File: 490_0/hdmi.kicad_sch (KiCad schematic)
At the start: 6 parts, among them J19 467650301, U10 EMI8142MUTAG, U13 SP3003-02XTG, U14 SP3003-02XTG, U9 EMI8142MUTAG

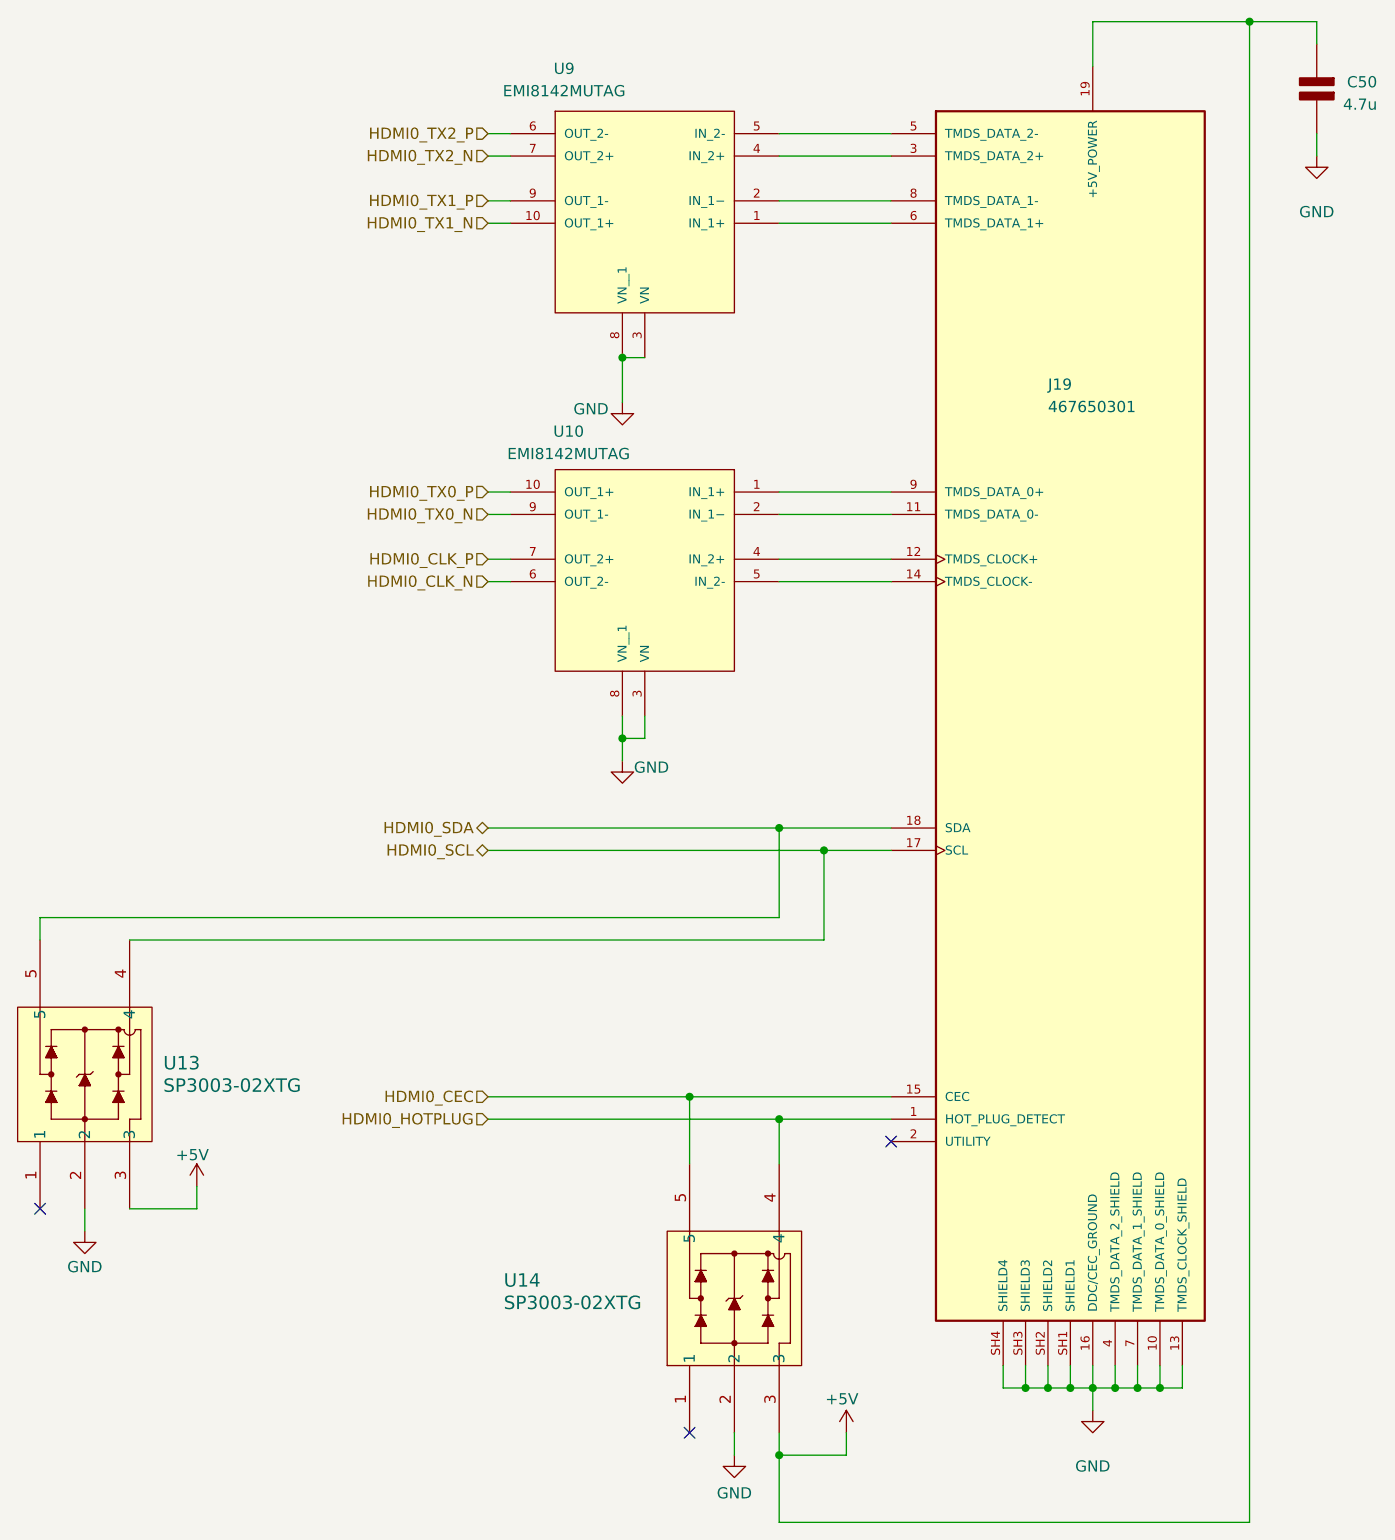
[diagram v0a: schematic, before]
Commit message: Changed microHDMI to normal HDMI because of the footprint
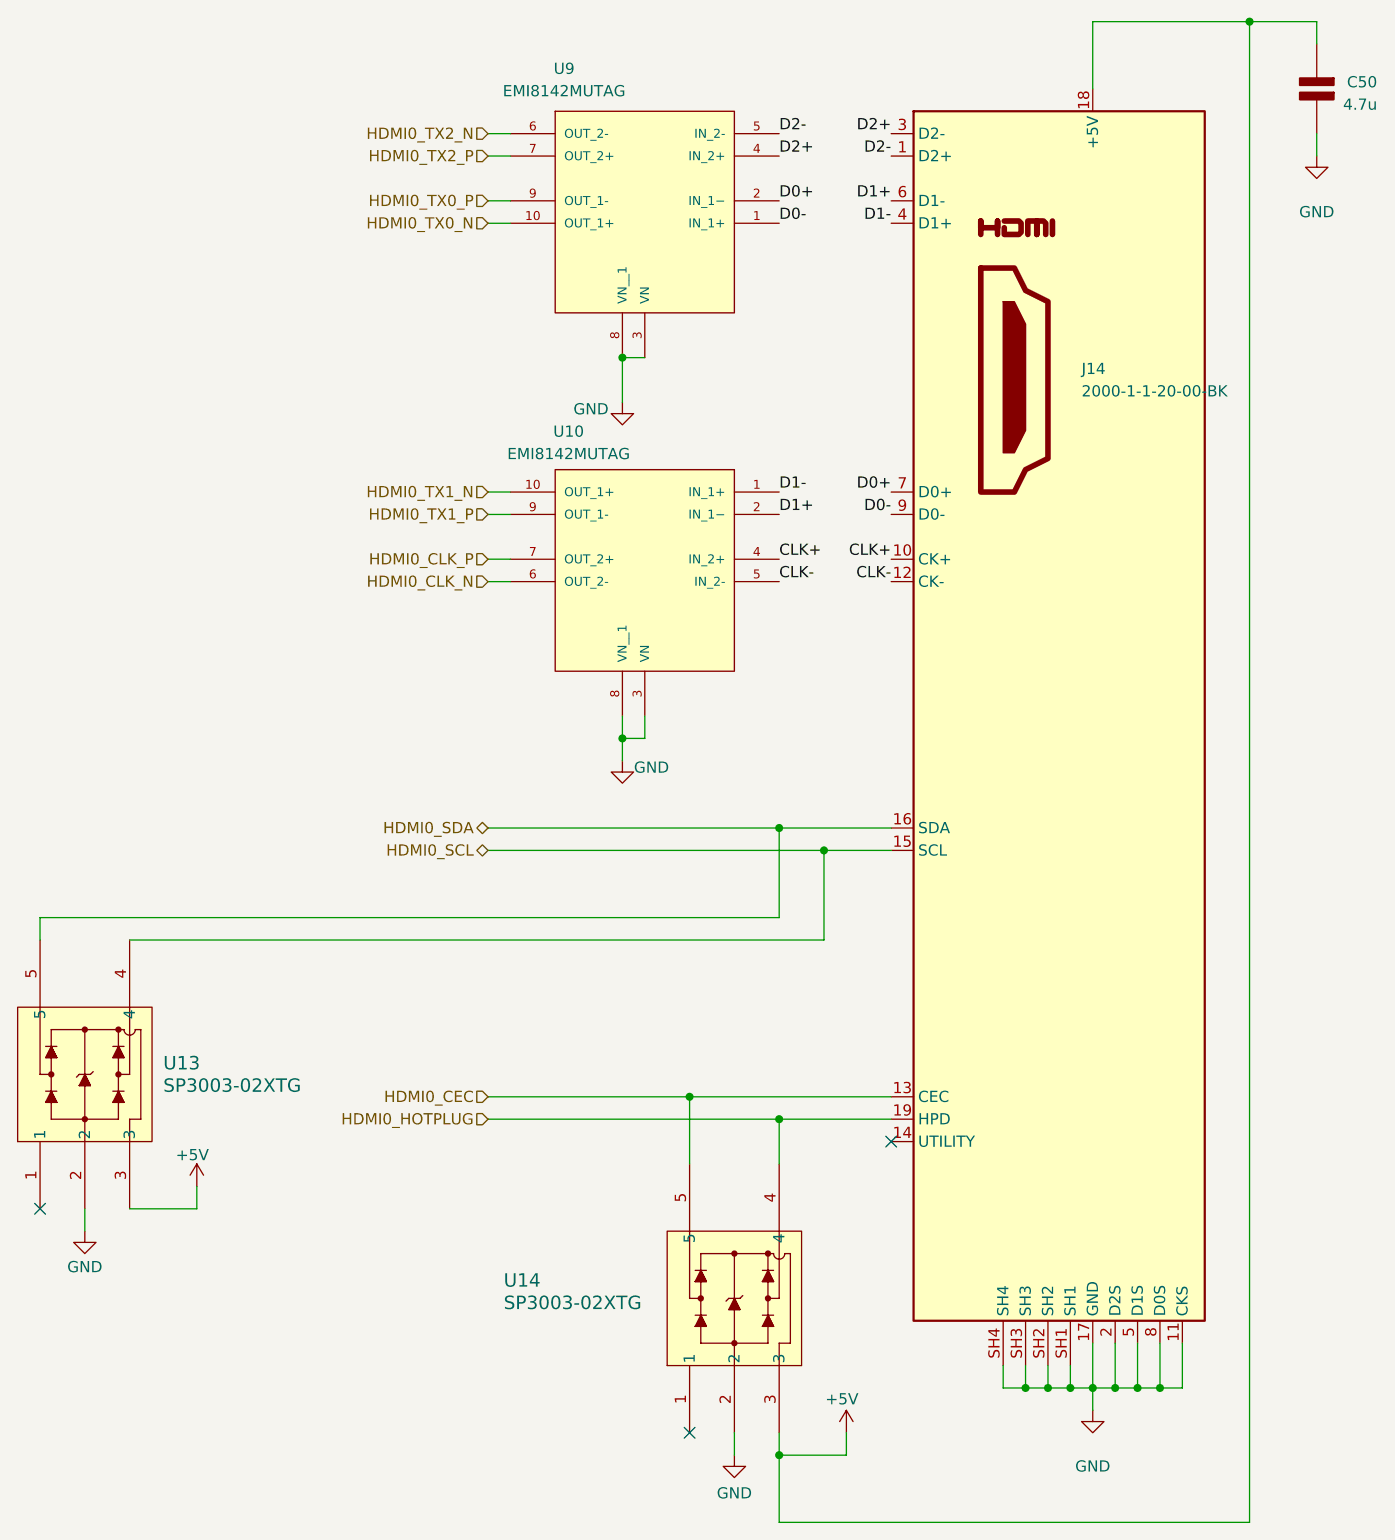
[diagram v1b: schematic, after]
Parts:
- removed J19: 467650301, *CapStone*:MOLEX_467650301, symbol capstone_parts:467650301
- added J14: 2000-1-1-20-00-BK, *CapStone*:CNCTECH_2000-1-1-20-00-BK, symbol capstone_parts:HDMI_A
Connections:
- net +5V: now also J14.18 (+5V)
- net GND: now also J14.11 (CKS), J14.17 (GND), J14.2 (D2S), J14.5 (D1S), J14.8 (D0S), J14.SH1, J14.SH2, J14.SH3, J14.SH4
- net HDMI0_CEC: now also J14.13 (CEC)
- net HDMI0_HOTPLUG: now also J14.19 (HPD)
- net HDMI0_SCL: now also J14.15 (SCL)
- net HDMI0_SDA: now also J14.16 (SDA)
- net HDMI0_TX0_N: now also U9.10 (OUT_1+); no longer U10.9 (OUT_1-)
- net HDMI0_TX0_P: now also U9.9 (OUT_1-); no longer U10.10 (OUT_1+)
- net HDMI0_TX1_N: now also U10.10 (OUT_1+); no longer U9.10 (OUT_1+)
- net HDMI0_TX1_P: now also U10.9 (OUT_1-); no longer U9.9 (OUT_1-)
- net HDMI0_TX2_N: now also U9.6 (OUT_2-); no longer U9.7 (OUT_2+)
- net HDMI0_TX2_P: now also U9.7 (OUT_2+); no longer U9.6 (OUT_2-)
- net D1+: now reaches U10.2 (IN_1−)
- net D1+: now also J14.6 (D1-)
- net CLK+: now reaches U10.4 (IN_2+)
- net CLK+: now also J14.10 (CK+)
- net CLK-: now reaches U10.5 (IN_2-)
- net CLK-: now also J14.12 (CK-)
- net D2+: now reaches U9.4 (IN_2+)
- net D2+: now also J14.3 (D2-)
- net D2-: now reaches U9.5 (IN_2-)
- net D2-: now also J14.1 (D2+)
- net D0-: now reaches U9.1 (IN_1+)
- net D0-: now also J14.9 (D0-)
- net D0+: now reaches U9.2 (IN_1−)
- net D0+: now also J14.7 (D0+)
- net D1-: now reaches U10.1 (IN_1+)
- net D1-: now also J14.4 (D1+)

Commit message: Routing ESD to 100 pin connector
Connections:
- net HDMI0_CEC: now also U13.4; no longer U14.5
- net HDMI0_SCL: now also U14.5; no longer U13.4
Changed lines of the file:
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@@
+	)
+	(junction
+		(at 134.62 170.18)
+		(diameter 0)
+		(color 0 0 0 0)
+	)
+	(junction
+		(at 101.6 177.8)
+		(diameter 0)
+		(color 0 0 0 0)
+	)
+	(junction
+		(at 81.28 137.16)
+		(diameter 0)
+		(color 0 0 0 0)
 	)
 	(junction
@@
 		(color 0 0 0 0)
 	)
-	(junction
-		(at 134.62 170.18)
-		(diameter 0)
-		(color 0 0 0 0)
-	)
-	(junction
-		(at 101.6 177.8)
-		(diameter 0)
-		(color 0 0 0 0)
-	)
-	(junction
-		(at 91.44 137.16)
-		(diameter 0)
-		(color 0 0 0 0)
-	)
 	(no_connect
 		(at 91.44 175.26)
@@
 	(wire
 		(pts
-			(xy 91.44 137.16) (xy 114.3 137.16)
-		)
-		(stroke
-			(width 0)
-			(type default)
-		)
-	)
-	(wire
-		(pts
 			(xy 147.32 170.18) (xy 144.78 170.18)
 		)
@@
 	(wire
 		(pts
-			(xy 106.68 119.38) (xy 106.68 109.22)
-		)
-		(stroke
-			(width 0)
-			(type default)
-		)
-	)
-	(wire
-		(pts
-			(xy 27.94 119.38) (xy 106.68 119.38)
+			(xy 106.68 133.35) (xy 91.44 133.35)
 		)
 		(stroke
@@
 	(wire
 		(pts
+			(xy 81.28 119.38) (xy 81.28 137.16)
+		)
+		(stroke
+			(width 0)
+			(type default)
+		)
+	)
+	(wire
+		(pts
+			(xy 81.28 137.16) (xy 114.3 137.16)
+		)
+		(stroke
+			(width 0)
+			(type default)
+		)
+	)
+	(wire
+		(pts
 			(xy 101.6 185.42) (xy 101.6 177.8)
 		)
@@
 	(wire
 		(pts
-			(xy 68.58 137.16) (xy 91.44 137.16)
+			(xy 68.58 137.16) (xy 81.28 137.16)
+		)
+		(stroke
+			(width 0)
+			(type default)
+		)
+	)
+	(wire
+		(pts
+			(xy 91.44 133.35) (xy 91.44 144.78)
 		)
 		(stroke
@@
 	(wire
 		(pts
-			(xy 91.44 137.16) (xy 91.44 144.78)
-		)
-		(stroke
-			(width 0)
-			(type default)
-		)
-	)
-	(wire
-		(pts
 			(xy 101.6 139.7) (xy 114.3 139.7)
 		)
@@
 	(wire
 		(pts
+			(xy 106.68 109.22) (xy 106.68 133.35)
+		)
+		(stroke
+			(width 0)
+			(type default)
+		)
+	)
+	(wire
+		(pts
 			(xy 68.58 76.2) (xy 71.12 76.2)
 		)
@@
 	(wire
 		(pts
+			(xy 106.68 109.22) (xy 114.3 109.22)
+		)
+		(stroke
+			(width 0)
+			(type default)
+		)
+	)
+	(wire
+		(pts
+			(xy 27.94 119.38) (xy 81.28 119.38)
+		)
+		(stroke
+			(width 0)
+			(type default)
+		)
+	)
+	(wire
+		(pts
 			(xy 83.82 99.06) (xy 83.82 96.52)
 		)
@@
 		)
 		(stroke
-			(width 0)
-			(type default)
-		)
-	)
-	(wire
-		(pts
-			(xy 106.68 109.22) (xy 114.3 109.22)
-		)
-		(stroke

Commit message: Friday, March 20th: PCB Final for BOM
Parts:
- J14: footprint *CapStone*:CNCTECH_2000-1-1-20-00-BK -> capstone:CNCTECH_2000-1-1-20-00-BK
- U10, U9: footprint *CapStone*:SON40P220X135X50-10N_EMI8142MUTAG -> capstone:SON40P220X135X50-10N_EMI8142MUTAG
- U13, U14: footprint *CapStone*:SOT553_LTF_SP3003_02XTG -> capstone:SOT553_LTF_SP3003_02XTG
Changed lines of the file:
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@@
 			)
 		)
-		(property "Footprint" "*CapStone*:SOT553_LTF_SP3003_02XTG"
+		(property "Footprint" "capstone:SOT553_LTF_SP3003_02XTG"
 			(at 17.78 149.86 0)
 			(effects
@@
 		)
 		(property "Voltage Rating" ""
+			(at 17.78 149.86 90)
+			(effects
+				(font
+					(size 1.27 1.27)
+				)
+				(hide yes)
+			)
+		)
+		(property "OPTION" ""
 			(at 17.78 149.86 90)
 			(effects
@@
 			)
 		)
-		(property "Footprint" "*CapStone*:CNCTECH_2000-1-1-20-00-BK"
+		(property "Footprint" "capstone:CNCTECH_2000-1-1-20-00-BK"
 			(at 125.095 55.88 0)
 			(effects
@@
 		)
 		(property "Unit" "pcs"
+			(at 124.46 55.88 0)
+			(effects
+				(font
+					(size 1.27 1.27)
+				)
+				(hide yes)
+			)
+		)
+		(property "OPTION" ""
 			(at 124.46 55.88 0)
 			(effects
@@
 			)
 		)
+		(property "OPTION" ""
+			(at 162.56 22.86 0)
+			(effects
+				(font
+					(size 1.27 1.27)
+				)
+				(hide yes)
+			)
+		)
 		(pin "2"
 		)
@@
 			)
 		)
-		(property "Footprint" "*CapStone*:SOT553_LTF_SP3003_02XTG"
+		(property "Footprint" "capstone:SOT553_LTF_SP3003_02XTG"
 			(at 91.44 175.26 0)
 			(effects
@@
 		)
 		(property "Voltage Rating" ""
+			(at 91.44 175.26 90)
+			(effects
+				(font
+					(size 1.27 1.27)
+				)
+				(hide yes)
+			)
+		)
+		(property "OPTION" ""
 			(at 91.44 175.26 90)
 			(effects
@@
 			)
 		)
-		(property "Footprint" "*CapStone*:SON40P220X135X50-10N_EMI8142MUTAG"
+		(property "Footprint" "capstone:SON40P220X135X50-10N_EMI8142MUTAG"
 			(at 86.36 35.56 0)
 			(effects
@@
 		)
 		(property "Voltage Rating" ""
+			(at 86.36 38.1 0)
+			(effects
+				(font
+					(size 1.27 1.27)
+				)
+				(hide yes)
+			)
+		)
+		(property "OPTION" ""
 			(at 86.36 38.1 0)
 			(effects
@@
 			)
 		)
-		(property "Footprint" "*CapStone*:SON40P220X135X50-10N_EMI8142MUTAG"
+		(property "Footprint" "capstone:SON40P220X135X50-10N_EMI8142MUTAG"
 			(at 86.36 76.2 0)
 			(effects
@@
 			(at 86.36 78.74 0)
 			(effects
+				(font
+					(size 1.27 1.27)
+				)
+				(hide yes)
+			)
+		)
+		(property "OPTION" ""
+			(at 86.36 78.74 0)
+			(effects
